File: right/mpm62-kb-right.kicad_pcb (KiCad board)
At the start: 2 copper layers, 86 parts, among them J1 Conn_02x08_Counter_Clockwise, SW1 SW_Push, U1 ATmega32U4-AU, Y1 16MHz

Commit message: Right pcb complete
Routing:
- net ROW1: track 163.0 -> 334.8 mm, vias 2 -> 14
- net Net-(R4-Pad2): track 17.4 -> 128.1 mm, vias 0 -> 4
- net ROW3: track 108.9 -> 184.1 mm, vias 3 -> 5
- net ROW2: track 165.8 -> 235.7 mm, vias 7 -> 11
- net Net-(USB1-Pad6): track 0.00 -> 16.3 mm
- net Net-(D15-Pad2): track 0.00 -> 7.63 mm
- net +5V: track 242.7 -> 247.1 mm, vias 6 -> 5

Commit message: Minor pcb cleanup near crystal.
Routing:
- net COL12: track 111.1 -> 119.0 mm
- net ROW0: track 360.9 -> 362.0 mm
- net COL8: vias 10 -> 8
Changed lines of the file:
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@@
     (thickness 1.6)
     (drawings 0)
-    (tracks 1043)
+    (tracks 1045)
     (zones 0)
     (modules 86)
@@
   )
   (segment (start 162.727498 127.42) (end 163.025 127.42) (width 0.375) (layer B.Cu) (net 1))
-  (segment (start 161.027498 129.12) (end 162.727498 127.42) (width 0.375) (layer B.Cu) (net 1))
   (segment (start 160.825 129.12) (end 161.027498 129.12) (width 0.375) (layer B.Cu) (net 1))
   (segment (start 160.7375 129.2075) (end 160.825 129.12) (width 0.375) (layer B.Cu) (net 1))
   (segment (start 157.734 129.2075) (end 160.7375 129.2075) (width 0.375) (layer B.Cu) (net 1))
   (segment (start 165.049 126.5195) (end 165.862 127.3325) (width 0.375) (layer B.Cu) (net 1))
-  (segment (start 160.925 129.12) (end 160.825 129.12) (width 0.375) (layer B.Cu) (net 1))
   (segment (start 162.488 130.683) (end 160.925 129.12) (width 0.375) (layer B.Cu) (net 1))
   (segment (start 167.513 129.921) (end 166.751 130.683) (width 0.375) (layer B.Cu) (net 1))
@@
   (segment (start 184.553153 125.035847) (end 183.388 126.201) (width 0.375) (layer B.Cu) (net 1))
   (segment (start 184.608153 125.035847) (end 184.553153 125.035847) (width 0.375) (layer B.Cu) (net 1))
+  (segment (start 160.925 129.12) (end 160.825 129.12) (width 0.375) (layer B.Cu) (net 1))
+  (segment (start 162.925 127.42) (end 163.025 127.42) (width 0.25) (layer B.Cu) (net 1))
+  (segment (start 161.925 128.27) (end 162.925 127.42) (width 0.25) (layer B.Cu) (net 1))
+  (segment (start 160.825 129.12) (end 161.925 128.27) (width 0.25) (layer B.Cu) (net 1))
   (segment (start 167.259263 105.361763) (end 167.8155 105.918) (width 0.375) (layer B.Cu) (net 2))
   (segment (start 164.084 102.1865) (end 167.259263 105.361763) (width 0.375) (layer B.Cu) (net 2))
@@
   (segment (start 198.883 59.309) (end 198.882 59.308) (width 0.25) (layer B.Cu) (net 11))
   (segment (start 201.422 59.309) (end 198.883 59.309) (width 0.25) (layer B.Cu) (net 11))
-  (segment (start 157.19715 130.175) (end 161.255202 130.175) (width 0.25) (layer B.Cu) (net 11))
-  (segment (start 156.70899 129.68684) (end 157.19715 130.175) (width 0.25) (layer B.Cu) (net 11))
-  (segment (start 156.70899 126.85316) (end 156.70899 129.68684) (width 0.25) (layer B.Cu) (net 11))
-  (segment (start 157.19715 126.365) (end 156.70899 126.85316) (width 0.25) (layer B.Cu) (net 11))
-  (segment (start 160.39359 126.365) (end 157.19715 126.365) (width 0.25) (layer B.Cu) (net 11))
-  (segment (start 162.649 124.10959) (end 160.39359 126.365) (width 0.25) (layer B.Cu) (net 11))
-  (segment (start 162.649 120.762) (end 162.649 124.10959) (width 0.25) (layer B.Cu) (net 11))
   (via (at 167.259 135.128) (size 0.8) (drill 0.4) (layers F.Cu B.Cu) (net 11))
-  (segment (start 162.275712 131.19551) (end 163.32651 131.19551) (width 0.25) (layer B.Cu) (net 11))
-  (segment (start 163.32651 131.19551) (end 167.259 135.128) (width 0.25) (layer B.Cu) (net 11))
-  (segment (start 161.255202 130.175) (end 162.275712 131.19551) (width 0.25) (layer B.Cu) (net 11))
   (via (at 172.503 140.552) (size 0.8) (drill 0.4) (layers F.Cu B.Cu) (net 11))
   (segment (start 172.503 140.372) (end 172.503 140.552) (width 0.25) (layer F.Cu) (net 11))
   (segment (start 167.259 135.128) (end 172.503 140.372) (width 0.25) (layer F.Cu) (net 11))
   (segment (start 172.503 140.552) (end 185.387002 140.552) (width 0.25) (layer B.Cu) (net 11))
+  (segment (start 158.23099 126.18001) (end 158.0674 126.18001) (width 0.25) (layer B.Cu) (net 11))
+  (segment (start 162.649 121.762) (end 158.23099 126.18001) (width 0.25) (layer B.Cu) (net 11))
+  (segment (start 162.649 120.762) (end 162.649 121.762) (width 0.25) (layer B.Cu) (net 11))
+  (segment (start 158.0674 126.18001) (end 156.14099 126.18001) (width 0.25) (layer B.Cu) (net 11))
+  (segment (start 155.702 126.619) (end 155.702 129.53859) (width 0.25) (layer B.Cu) (net 11))
+  (segment (start 156.14099 126.18001) (end 155.702 126.619) (width 0.25) (layer B.Cu) (net 11))
+  (segment (start 157.215409 131.051999) (end 160.515999 131.051999) (width 0.25) (layer B.Cu) (net 11))
+  (segment (start 155.702 129.53859) (end 157.215409 131.051999) (width 0.25) (layer B.Cu) (net 11))
+  (segment (start 167.259 135.128) (end 167.259 135.56699) (width 0.25) (layer B.Cu) (net 11))
+  (segment (start 162.61799 133.15399) (end 165.28499 133.15399) (width 0.25) (layer B.Cu) (net 11))
+  (segment (start 165.28499 133.15399) (end 167.259 135.128) (width 0.25) (layer B.Cu) (net 11))
+  (segment (start 160.515999 131.051999) (end 162.61799 133.15399) (width 0.25) (layer B.Cu) (net 11))
   (segment (start 79.864999 72.244999) (end 78.74 71.12) (width 0.25) (layer B.Cu) (net 12))
   (segment (start 82.678 75.058) (end 79.864999 72.244999) (width 0.25) (layer B.Cu) (net 12))
@@
   (via (at 107.442 135.001) (size 0.8) (drill 0.4) (layers F.Cu B.Cu) (net 56))
   (segment (start 109.982 137.541) (end 107.442 135.001) (width 0.25) (layer F.Cu) (net 56))
-  (segment (start 137.607214 138.308429) (end 135.768429 138.308429) (width 0.25) (layer F.Cu) (net 56))
-  (segment (start 135.768429 138.308429) (end 135.001 137.541) (width 0.25) (layer F.Cu) (net 56))
   (via (at 135.001 137.413999) (size 0.8) (drill 0.4) (layers F.Cu B.Cu) (net 56))
-  (segment (start 135.001 137.541) (end 135.001 137.413999) (width 0.25) (layer F.Cu) (net 56))
   (via (at 86.995 117.795) (size 0.8) (drill 0.4) (layers F.Cu B.Cu) (net 56))
-  (segment (start 152.908 137.668) (end 152.4 138.176) (width 0.25) (layer B.Cu) (net 56))
-  (via (at 137.607214 138.308429) (size 0.8) (drill 0.4) (layers F.Cu B.Cu) (net 56))
   (segment (start 110.109001 137.413999) (end 109.982 137.541) (width 0.25) (layer B.Cu) (net 56))
-  (segment (start 152.4 138.176) (end 137.739643 138.176) (width 0.25) (layer B.Cu) (net 56))
-  (segment (start 137.739643 138.176) (end 137.607214 138.308429) (width 0.25) (layer B.Cu) (net 56))
   (via (at 109.982 137.541) (size 0.8) (drill 0.4) (layers F.Cu B.Cu) (net 56))
   (segment (start 135.001 137.413999) (end 110.109001 137.413999) (width 0.25) (layer B.Cu) (net 56))
-  (via (at 152.908 137.668) (size 0.8) (drill 0.4) (layers F.Cu B.Cu) (net 56))
-  (segment (start 153.162 137.414) (end 152.908 137.668) (width 0.25) (layer F.Cu) (net 56))
-  (segment (start 156.21 137.414) (end 153.162 137.414) (width 0.25) (layer F.Cu) (net 56))
   (segment (start 86.995 121.031) (end 86.995 117.795) (width 0.25) (layer B.Cu) (net 56))
   (segment (start 100.965 135.001) (end 86.995 121.031) (width 0.25) (layer B.Cu) (net 56))
@@
   (segment (start 156.374 137.578) (end 156.21 137.414) (width 0.25) (layer B.Cu) (net 56))
   (segment (start 185.181997 127.746003) (end 185.181997 137.30335) (width 0.25) (layer B.Cu) (net 56))
+  (segment (start 153.162 137.414) (end 156.21 137.414) (width 0.25) (layer F.Cu) (net 56))
+  (segment (start 135.768429 138.308429) (end 152.267571 138.308429) (width 0.25) (layer F.Cu) (net 56))
+  (segment (start 152.267571 138.308429) (end 153.162 137.414) (width 0.25) (layer F.Cu) (net 56))
+  (segment (start 135.001 137.541) (end 135.768429 138.308429) (width 0.25) (layer F.Cu) (net 56))
+  (segment (start 135.001 137.413999) (end 135.001 137.541) (width 0.25) (layer F.Cu) (net 56))
   (segment (start 100.965 64.135) (end 110.49 73.66) (width 0.25) (layer F.Cu) (net 57))
   (segment (start 100.965 54.61) (end 100.965 64.135) (width 0.25) (layer F.Cu) (net 57))
@@
   (segment (start 158.115 62.23) (end 158.115 54.61) (width 0.25) (layer F.Cu) (net 60))
   (segment (start 167.64 71.755) (end 158.115 62.23) (width 0.25) (layer F.Cu) (net 60))
-  (via (at 155.408 116.737) (size 0.8) (drill 0.4) (layers F.Cu B.Cu) (net 60))
-  (segment (start 155.483 116.662) (end 155.408 116.737) (width 0.25) (layer B.Cu) (net 60))
-  (segment (start 157.749 116.662) (end 155.483 116.662) (width 0.25) (layer B.Cu) (net 60))
-  (segment (start 164.883202 130.81) (end 170.02125 130.81) (width 0.25) (layer F.Cu) (net 60))
-  (segment (start 155.408 121.334798) (end 164.883202 130.81) (width 0.25) (layer F.Cu) (net 60))
-  (segment (start 155.408 116.737) (end 155.408 121.334798) (width 0.25) (layer F.Cu) (net 60))
   (segment (start 170.02125 130.81) (end 170.02125 130.71475) (width 0.25) (layer F.Cu) (net 60))
   (via (at 175.445847 122.496153) (size 0.8) (drill 0.4) (layers F.Cu B.Cu) (net 60))
@@
   (segment (start 173.267251 118.149251) (end 173.521251 118.403251) (width 0.25) (layer F.Cu) (net 60))
   (segment (start 173.267251 106.427479) (end 173.267251 118.149251) (width 0.25) (layer F.Cu) (net 60))
+  (via (at 154.559 116.587) (size 0.8) (drill 0.4) (layers F.Cu B.Cu) (net 60))
+  (segment (start 154.634 116.662) (end 154.559 116.587) (width 0.25) (layer B.Cu) (net 60))
+  (segment (start 157.749 116.662) (end 154.634 116.662) (width 0.25) (layer B.Cu) (net 60))
+  (segment (start 152.273 118.873) (end 154.559 116.587) (width 0.25) (layer F.Cu) (net 60))
+  (segment (start 152.273 124.968) (end 152.273 118.873) (width 0.25) (layer F.Cu) (net 60))
+  (segment (start 155.829 128.524) (end 152.273 124.968) (width 0.25) (layer F.Cu) (net 60))
+  (segment (start 155.829 129.667) (end 155.829 128.524) (width 0.25) (layer F.Cu) (net 60))
+  (segment (start 156.972 130.81) (end 155.829 129.667) (width 0.25) (layer F.Cu) (net 60))
+  (segment (start 170.02125 130.81) (end 156.972 130.81) (width 0.25) (layer F.Cu) (net 60))
   (segment (start 193.83375 130.81) (end 193.83375 129.44475) (width 0.25) (layer F.Cu) (net 61))
   (segment (start 183.802748 92.71) (end 184.30875 92.71) (width 0.25) (layer F.Cu) (net 61))

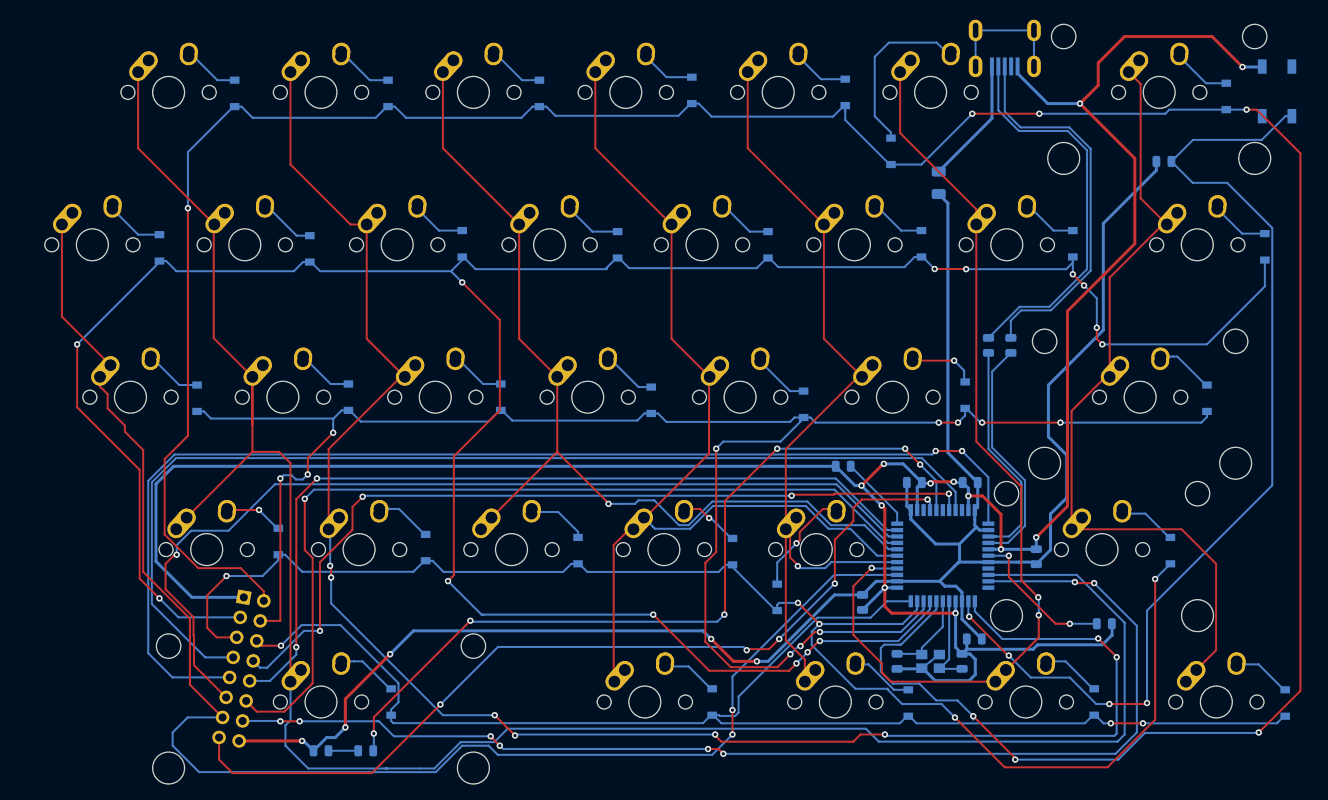
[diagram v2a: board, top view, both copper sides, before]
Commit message: Schematic and pre-routed right-side based on mcp23018
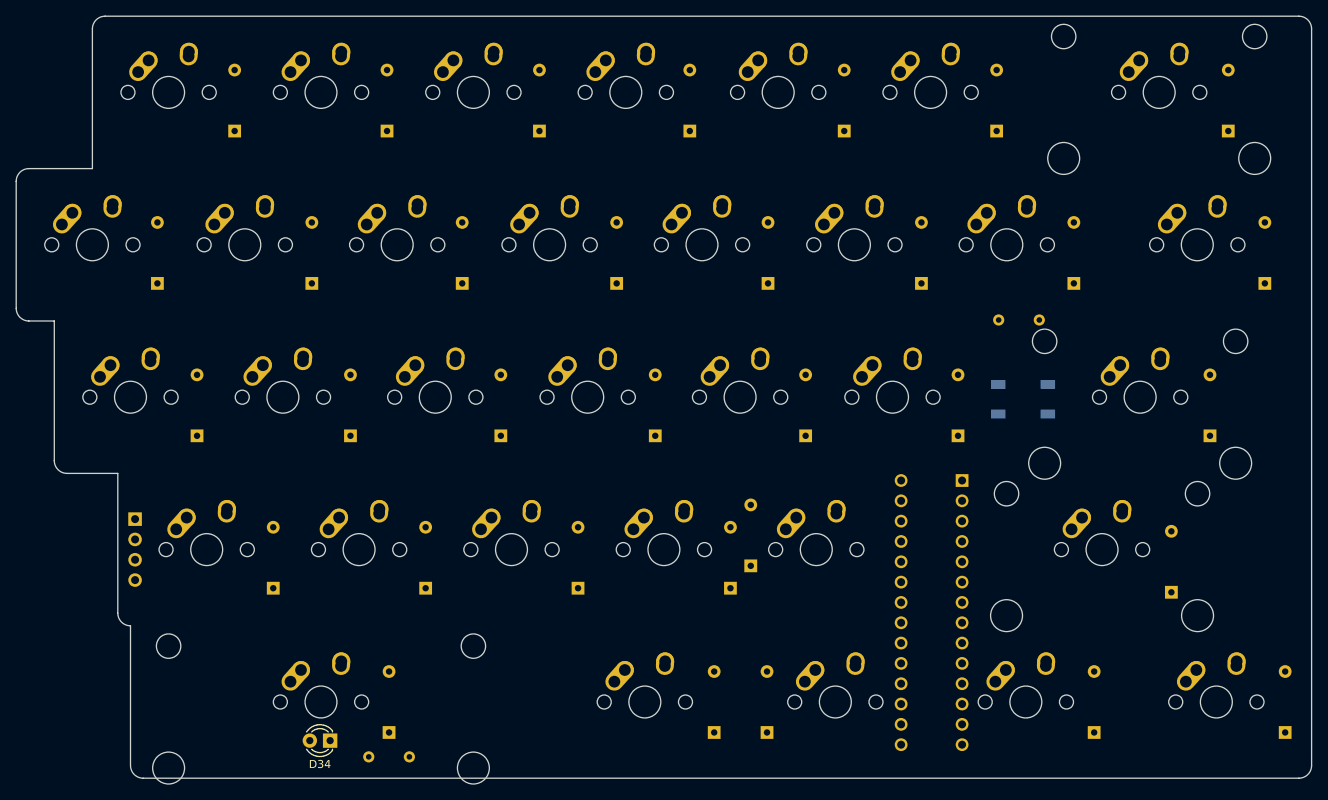
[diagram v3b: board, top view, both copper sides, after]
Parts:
- removed C1, C3, C4, C6: 0.1uF, Capacitor_SMD:C_0805_2012Metric
- removed C2, C5: 22pF, Capacitor_SMD:C_0805_2012Metric
- removed C7: 1uF, Capacitor_SMD:C_0805_2012Metric
- removed C8: 10uF, Capacitor_SMD:C_0805_2012Metric
- removed F1: 500mA, Fuse:Fuse_1206_3216Metric
- removed R3: 22, Resistor_SMD:R_0805_2012Metric
- removed R4: R_Small, Resistor_SMD:R_0805_2012Metric
- removed R5: 10k, Resistor_SMD:R_0805_2012Metric
- removed USB1: Molex-0548190589, random-keyboard-parts:Molex-0548190589
- removed Y1: 16MHz, Crystal:Crystal_SMD_3225-4Pin_3.2x2.5mm
- D1, D12, D13, D14, D15, D16, D17, D18, D19, D2, D20, D21, D22, D23, D24, D25, D26, D27, D28, D29, D3, D30, D31, D32, D33, D4, D5, D6: footprint Diode_SMD:D_SOD-123 -> Diode_THT:D_DO-35_SOD27_P7.62mm_Horizontal
- D10: renamed from D11; footprint Diode_SMD:D_SOD-123 -> Diode_THT:D_DO-35_SOD27_P7.62mm_Horizontal
- D11: renamed from D7; footprint Diode_SMD:D_SOD-123 -> Diode_THT:D_DO-35_SOD27_P7.62mm_Horizontal
- D34: footprint LED_SMD:LED_0805_2012Metric -> LED_THT:LED_D3.0mm; moved to F.Cu
- D7: renamed from D8; footprint Diode_SMD:D_SOD-123 -> Diode_THT:D_DO-35_SOD27_P7.62mm_Horizontal
- D8: renamed from D9; footprint Diode_SMD:D_SOD-123 -> Diode_THT:D_DO-35_SOD27_P7.62mm_Horizontal
- D9: renamed from D10; footprint Diode_SMD:D_SOD-123 -> Diode_THT:D_DO-35_SOD27_P7.62mm_Horizontal
- J1: value Conn_02x08_Counter_Clockwise -> Conn_01x04_Male; footprint Connector_PinSocket_2.54mm:PinSocket_2x08_P2.54mm_Vertical -> Connector_PinHeader_2.54mm:PinHeader_1x04_P2.54mm_Vertical
- R1: footprint Resistor_SMD:R_0805_2012Metric -> Resistor_THT:R_Axial_DIN0204_L3.6mm_D1.6mm_P5.08mm_Vertical
- R2: value 22 -> R_Small; footprint Resistor_SMD:R_0805_2012Metric -> Resistor_THT:R_Axial_DIN0204_L3.6mm_D1.6mm_P5.08mm_Vertical
- U1: value ATmega32U4-AU -> MCP23018-E_SP; footprint Package_QFP:TQFP-44_10x10mm_P0.8mm -> digikey-footprints:DIP-28_W7.62mm
- moved SW1 49.9 mm to (173.5, 95.5), turned to 0 degrees
- moved D25 18.0 mm to (141.5, 137.2)
- moved J1 16.7 mm to (62.5, 110.5), turned to 180 degrees
- moved D26 13.5 mm to (170.2, 62.0)
- moved U1 9.70 mm to (165.9, 105.7)
- moved D6 5.88 mm to (79.8, 119.1)
- moved R1 5.51 mm to (96.8, 140.2), turned to 180 degrees
- moved D32 5.21 mm to (192.0, 119.6)
- moved D23 5.16 mm to (165.4, 100.1)
- moved D24 5.14 mm to (139.4, 116.3)
- moved D16 5.09 mm to (131.8, 62.0)
- moved D10 5.08 mm to (98.8, 119.1)
- moved D27 4.95 mm to (179.8, 81.0)
- moved D22 4.95 mm to (160.8, 81.0)
- moved D8 4.95 mm to (103.4, 81.0)
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- renumbered MX11 to MX10, MX7 to MX11, MX8 to MX7, MX9 to MX8, MX10 to MX9
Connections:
- D34 pad 2: +5V -> (no net)
- J1 pad 1: GND -> VCC
- J1 pad 2: ROW0 -> GND
- J1 pad 3: ROW1 -> Net-(J1-Pad3)
- J1 pad 4: ROW2 -> Net-(J1-Pad4)
- MX11 pad 1: COL7 -> COL8
- R1 pad 1: Net-(D34-Pad1) -> Net-(R1-Pad1)
- R1 pad 2: LED_FN -> Net-(D34-Pad1)
- R2 pad 1: Net-(R2-Pad1) -> VCC
- R2 pad 2: D- -> Net-(R2-Pad2)
- SW1 pad 2: Net-(R4-Pad2) -> Net-(R2-Pad2)
- U1 pad 1: COL2 -> GND
- U1 pad 10: LED_CAPS -> COL12
- U1 pad 11: COL13 -> VCC
- U1 pad 12: COL8 -> Net-(J1-Pad3)
- U1 pad 13: Net-(R4-Pad2) -> Net-(J1-Pad4)
- U1 pad 14: +5V -> (no net)
- U1 pad 16: Net-(C5-Pad2) -> Net-(R2-Pad2)
- U1 pad 17: Net-(C2-Pad2) -> (no net)
- U1 pad 18: ROW0 -> (no net)
- U1 pad 19: ROW1 -> (no net)
- U1 pad 2: +5V -> (no net)
- U1 pad 20: ROW2 -> Net-(R1-Pad1)
- U1 pad 21: ROW3 -> (no net)
- U1 pad 22: ROW4 -> COL11
- U1 pad 23: GND -> COL10
- U1 pad 24: +5V -> COL9
- U1 pad 25: COL6 -> COL8
- U1 pad 26: COL12 -> COL7
- U1 pad 27: COL11 -> COL6
- U1 pad 28: COL10 -> (no net)
- U1 pad 3: Net-(R2-Pad1) -> ROW0
- U1 pad 4: Net-(R3-Pad1) -> ROW1
- U1 pad 5: GND -> ROW2
- U1 pad 6: Net-(C7-Pad2) -> ROW3
- U1 pad 7: +5V -> ROW4
- U1 pad 8: Net-(U1-Pad8) -> (no net)
- U1 pad 9: COL7 -> (no net)
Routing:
- net ROW0: track 362.0 -> 0.00 mm, vias 7 -> 0
- net ROW1: track 334.8 -> 0.00 mm, vias 14 -> 0
- net GND: track 333.3 -> 0.00 mm, vias 12 -> 0
- net COL7: track 256.9 -> 0.00 mm
- net +5V: track 247.1 -> 0.00 mm, vias 5 -> 0
- net ROW2: track 235.7 -> 0.00 mm, vias 11 -> 0
- net COL8: track 215.0 -> 0.00 mm, vias 8 -> 0
- net COL6: track 185.0 -> 0.00 mm, vias 2 -> 0
- net ROW3: track 184.1 -> 0.00 mm, vias 5 -> 0
- net ROW4: track 173.8 -> 0.00 mm, vias 3 -> 0
- net LED_CAPS: track 148.9 -> 0.00 mm, vias 8 -> 0
- net COL2: track 146.7 -> 0.00 mm, vias 2 -> 0
- net COL0: track 133.9 -> 0.00 mm
- net Net-(R4-Pad2): track 128.1 -> 0.00 mm, vias 4 -> 0
- net COL10: track 123.4 -> 0.00 mm
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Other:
- board outline added: 161.9 x 95.2 mm
